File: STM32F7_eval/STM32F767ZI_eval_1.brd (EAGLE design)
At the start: 76.2 x 53.3 mm, 101 parts, among them CN3 GROVE-4P-CONN-I2C-90D, CN4 GROVE-4P-CONN-AN01-90D, CN5 ARDUINO_COMPAT_IF, CN6 STLINKV21_SWD_IF, CN7 WFT0750CZ09-SMD_, CN8 MCO_IF, CN9 UART_IF, Q1 PMF370XN_, SW1 SKRPACE010_, SW2 SKRPACE010_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

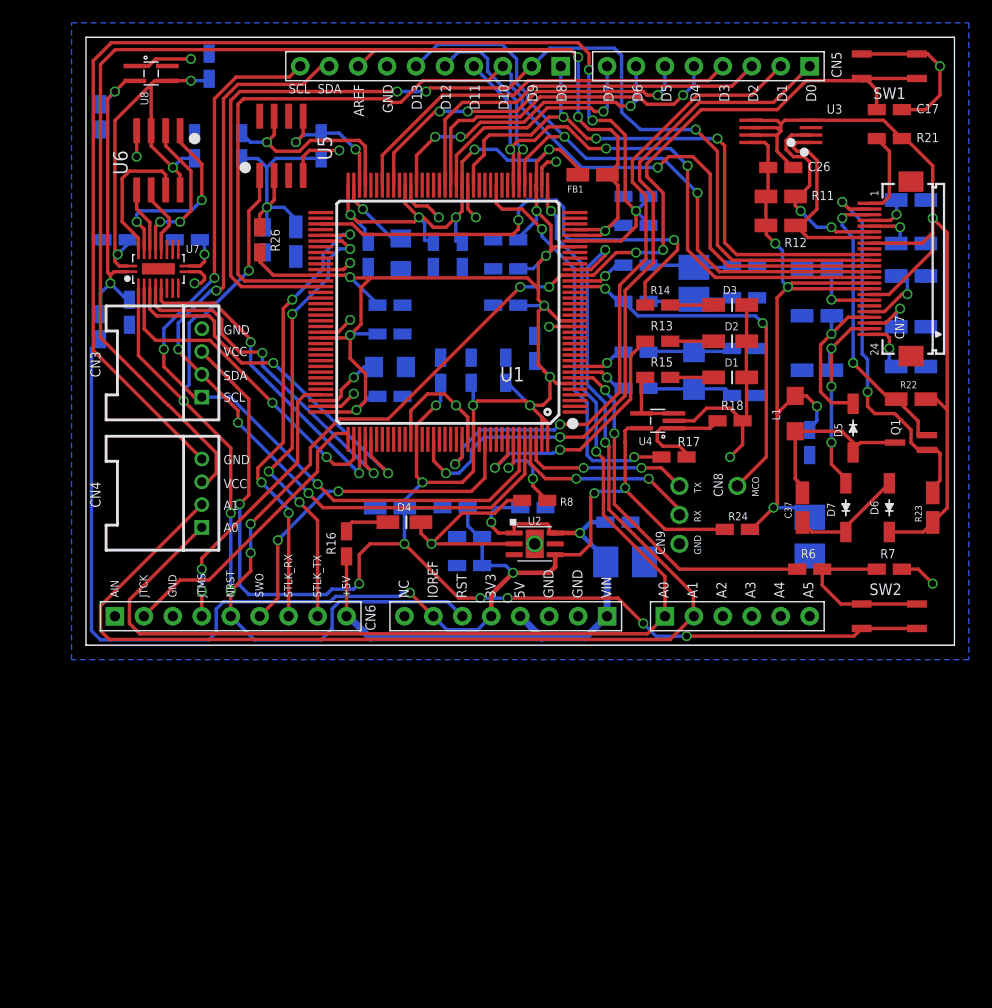
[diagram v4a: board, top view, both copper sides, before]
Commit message: 評価回路を修正
・配線を修正
・+1V8のNAMEが不正だったので修正
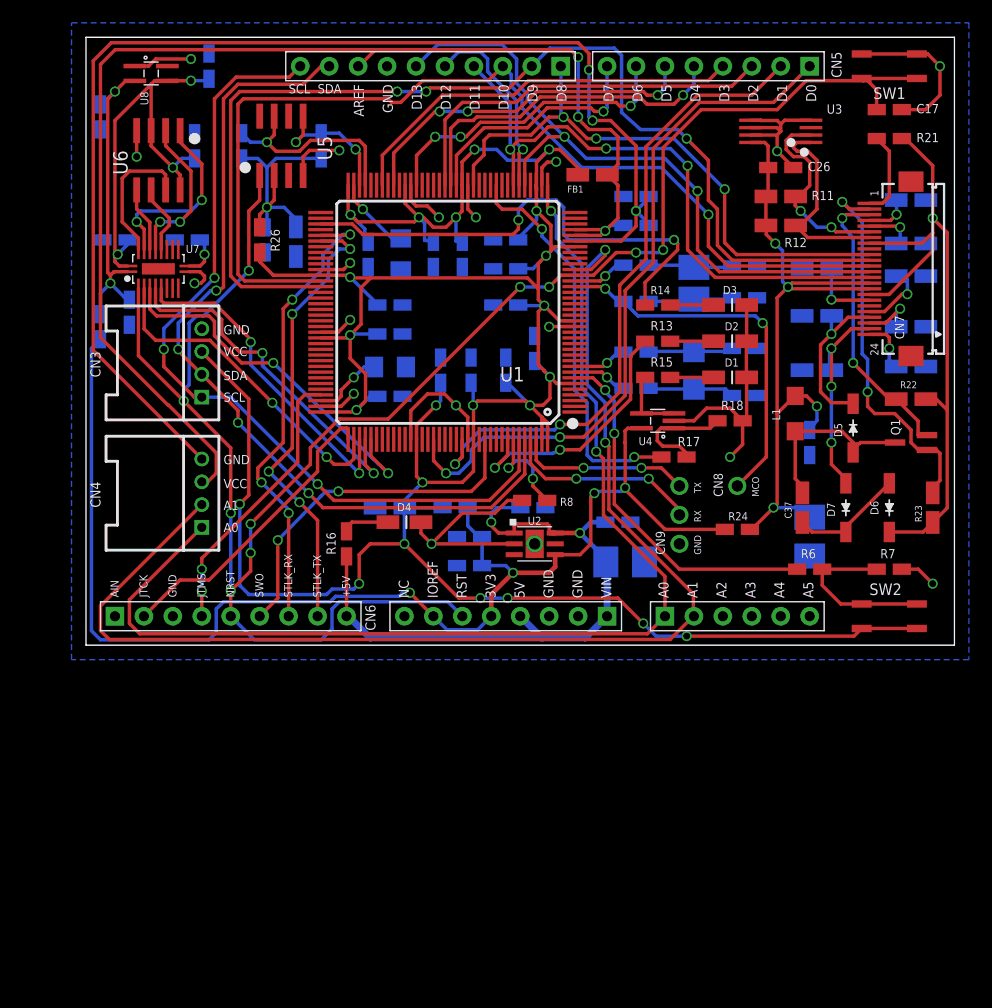
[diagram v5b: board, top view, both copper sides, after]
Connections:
- net +18V renamed +1V8
- net N$15 renamed !OE!
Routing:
- net 0V: track 189.1 -> 180.4 mm, vias 18 -> 19
- net PD14: track 92.5 -> 89.5 mm
- net PF12: track 53.5 -> 51.3 mm
- net NRST: track 171.2 -> 170.1 mm
- net PG9: track 62.9 -> 61.9 mm
- net PG14: track 58.2 -> 57.2 mm
- net PD15: track 97.1 -> 96.1 mm
- net TCK: track 26.1 -> 26.7 mm

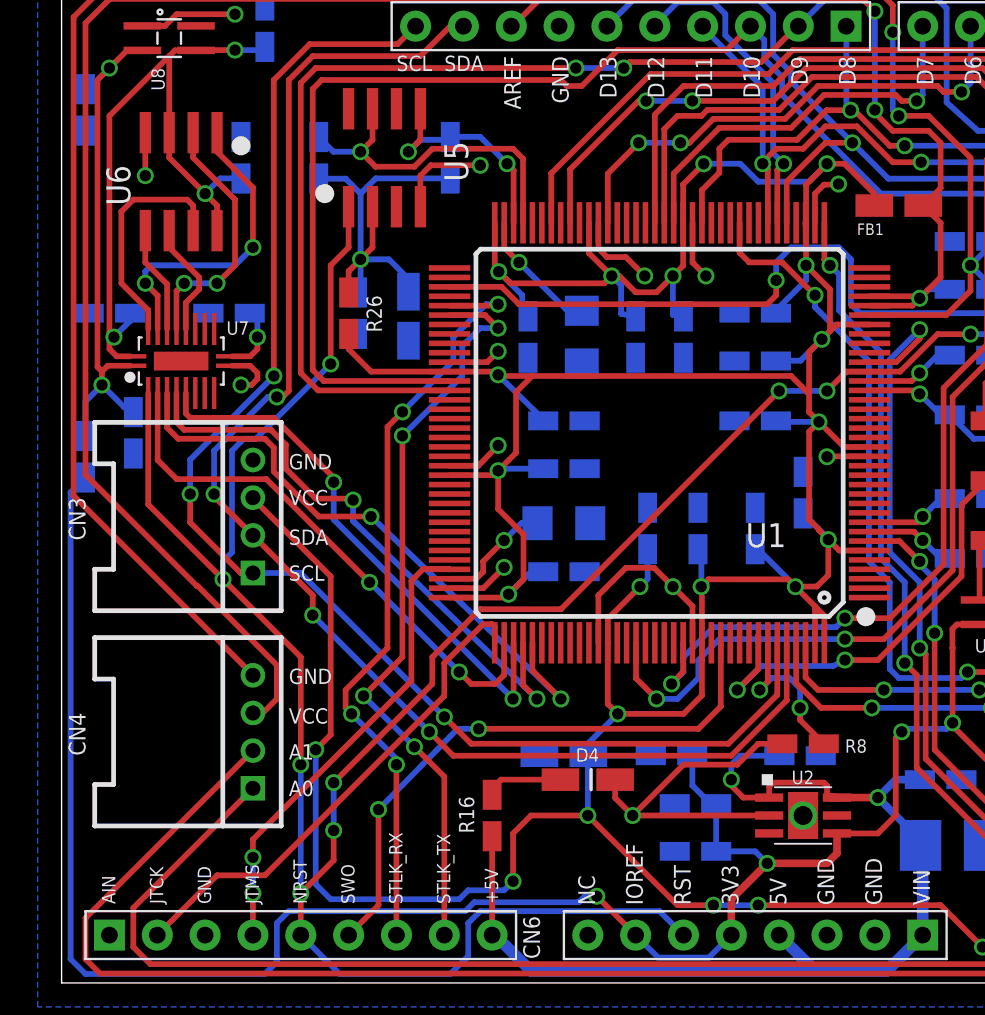
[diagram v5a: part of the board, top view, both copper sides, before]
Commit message: 評価回路を修正
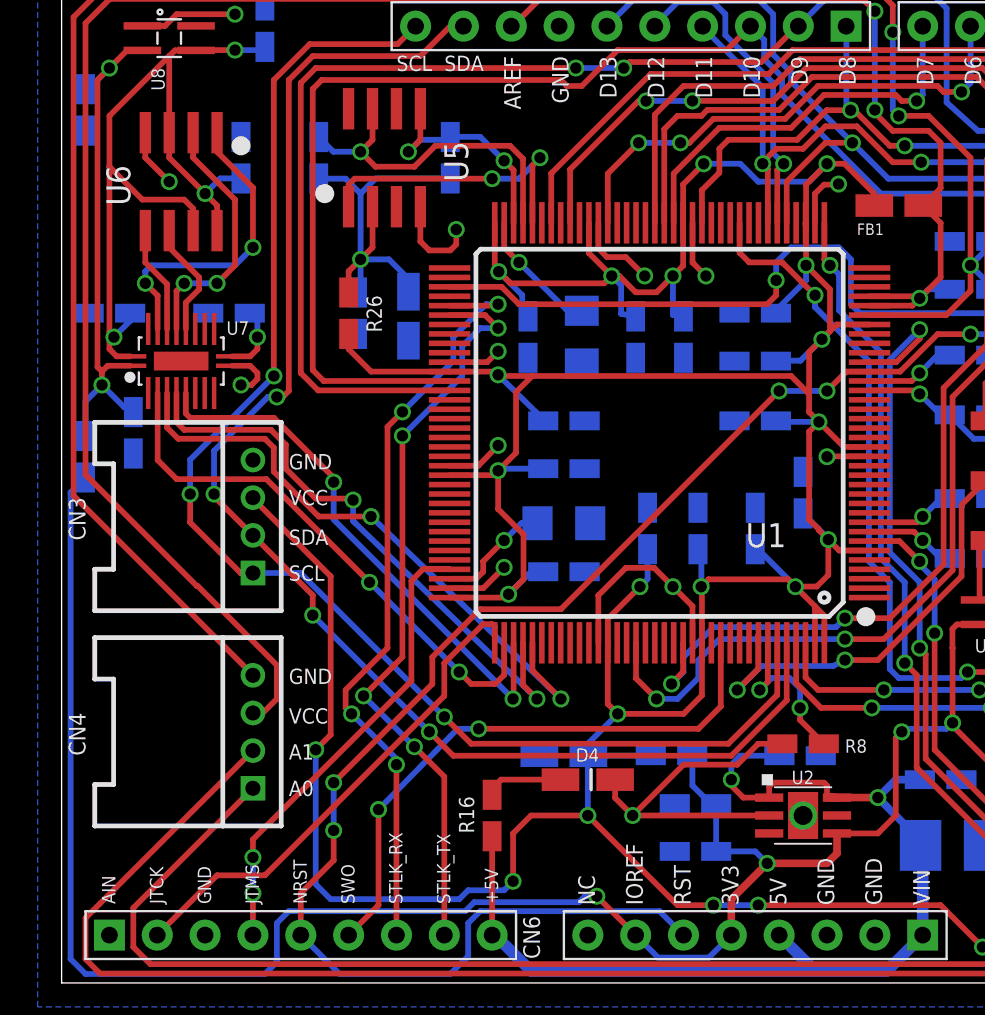
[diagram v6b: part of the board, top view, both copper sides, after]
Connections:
- removed net !RESET!: U6.7, U7.19
- new net PE15: U1.68, U5.1
- net +1V8: now also U6.7
- net NRST: no longer U5.1, U7.2
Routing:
- net NRST: track 170.1 -> 117.2 mm, vias 10 -> 6
- net PE15: track 0.00 -> 15.8 mm, vias 0 -> 2
- net !RESET!: track 12.4 -> 0.00 mm
- net +1V8: track 38.4 -> 44.9 mm
- net 0V: track 180.4 -> 181.1 mm

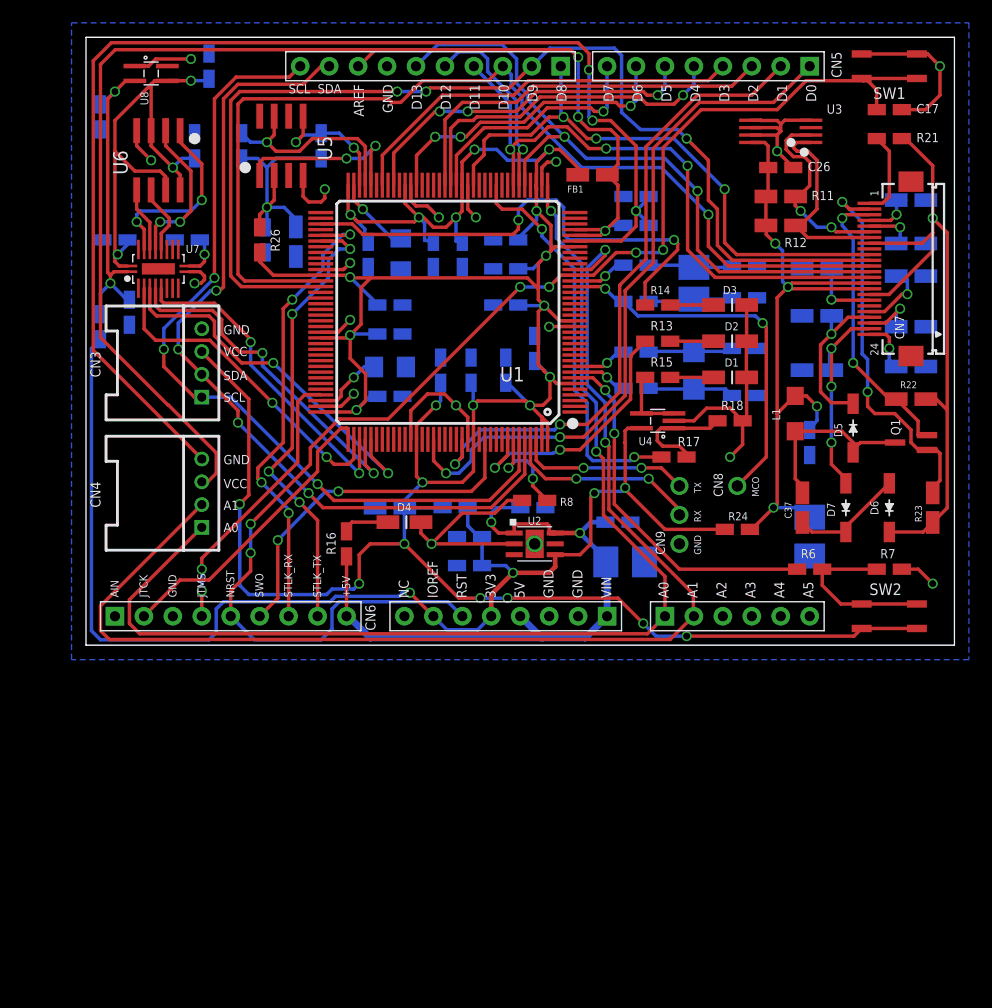
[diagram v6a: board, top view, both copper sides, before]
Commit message: 回路図を修正
・部品のパッケージを入れ替え
・セキュリティーチップ回路図のシートを移動
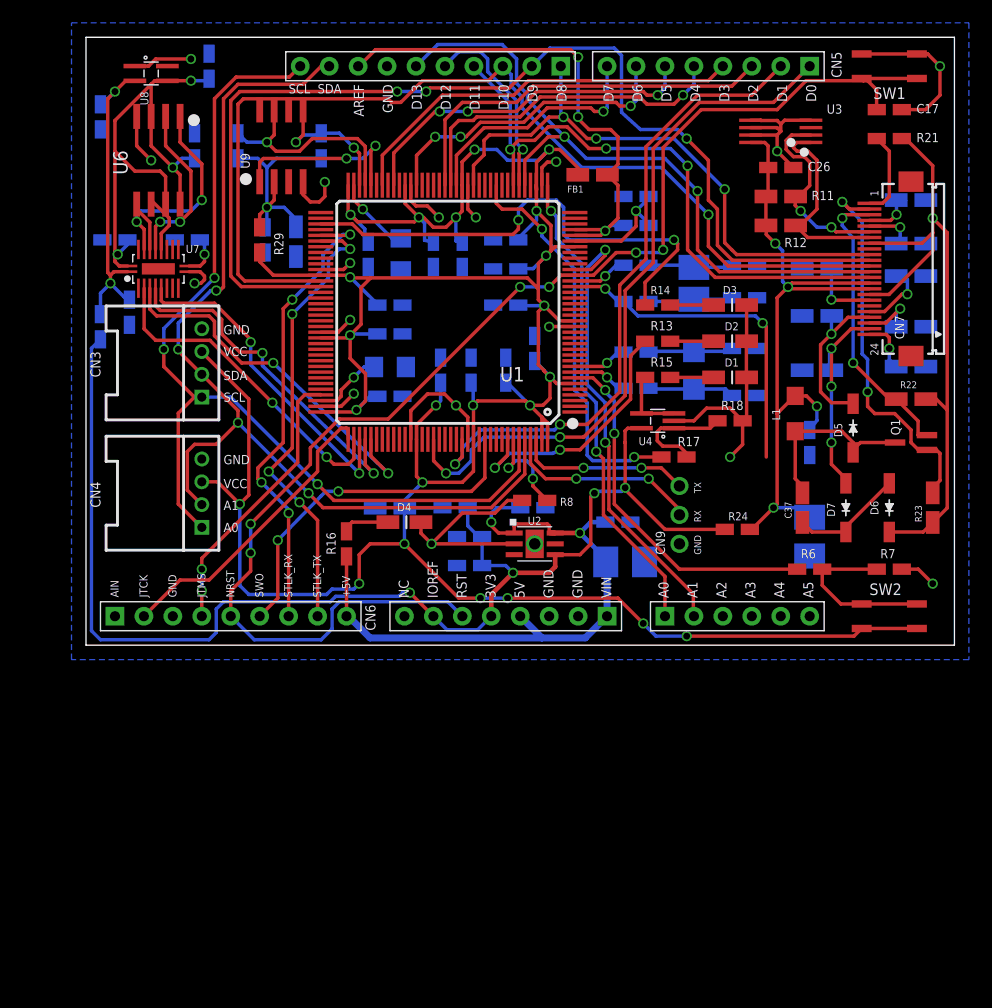
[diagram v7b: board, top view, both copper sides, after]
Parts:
- removed CN8: MCO_IF, PartsForProto:MCO_IF_1PIN
- removed R19: 3.3k, Parts:SMD_1608_DEV
- removed U5: STSAFE, Parts:SO8
- added R27: 3.3k, Parts:SMD_1608_DEV
- added U9: STSAFE, Parts:SO8N
- CN4: value GROVE-4P-CONN-AN01-90D -> GROVE-4P-CONN-I2C-90D
- U6: device Parts:SO8 -> Parts:SOP_8L
- renumbered C28 to C47, C29 to C48, R20 to R28, R26 to R29
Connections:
- net 0V: now also CN4.4, U9.4; no longer U5.4
- net AGND: no longer CN4.4
- net AVDD: no longer CN4.3
- net PA3: no longer CN4.1
- net PB10: now also R27.1, U9.7; no longer R19.1, U5.7
- net PB11: now also U9.5; no longer U5.5
- net PB8: now also CN4.1
- net PB9: now also CN4.2
- net PC0: no longer CN4.2
- net PE15: now also U9.1; no longer U5.1
- net PH0: no longer CN8.1
- net VCC_STSAFE: now also R27.2, U9.2; no longer R19.2, U5.2
- net VDD: now also CN4.3
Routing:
- net AGND: track 110.6 -> 10.7 mm, vias 3 -> 1
- net PC0: track 108.3 -> 40.4 mm
- net AVDD: track 112.9 -> 46.5 mm
- net PA3: track 101.1 -> 42.1 mm
- net PB8: track 73.9 -> 86.8 mm
- net PB9: track 75.7 -> 86.4 mm
- net VDD: track 277.9 -> 282.0 mm
- net PH0: track 33.3 -> 29.7 mm
- net +1V8: track 44.9 -> 47.4 mm
- net SO: track 13.7 -> 14.9 mm
- net SI: track 5.70 -> 4.45 mm
- net !CS!: track 16.5 -> 17.7 mm
- net 0V: track 181.1 -> 182.2 mm
- net PB10: track 18.2 -> 19.1 mm
- net PE15: track 15.8 -> 16.3 mm
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
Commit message: 回路図を修正
・構成部品を入替え
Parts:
- removed C43: 1uF, Parts:SMD_1608_DEV
- removed C44: 0.1uF, Parts:SMD_1608_DEV
- removed U8: NCP563, Parts:SC-70-4_DEV
- added C28, C49: 1uF X5R, Parts:SMD_1608_DEV
- added C29: 10uF, Parts:C1210_TPST_DEV
- added U5: MIC5366-1.8YC5_, Parts:SC-70-5_DEV
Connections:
- net !CS!: now also U7.3; no longer U7.18
- net +1V8: now also C28.1, C29.1, C45.1, U5.5, U7.1; no longer C44.1, C46.1, U7.20, U8.3
- net 0V: now also C28.2, C29.2, C49.2, U5.2; no longer C43.2, C44.2, U8.1
- net PA15: now also U7.18; no longer U7.3
- net PC10: now also U7.16; no longer U7.6
- net PC11: now also U7.14; no longer U7.5
- net PC12: now also U7.12; no longer U7.4
- net SCLK: now also U7.5; no longer U7.15
- net SI: now also U7.9; no longer U7.17
- net SO: now also U7.7; no longer U7.16
- net VCC_MEM: now also C46.1, C49.1, U5.1, U5.3, U7.20; no longer C43.1, C45.1, U7.1, U8.2
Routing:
- net VCC_MEM: track 28.2 -> 0.00 mm, vias 2 -> 0
- net +1V8: track 47.4 -> 40.9 mm, vias 3 -> 2
- net 0V: track 182.2 -> 176.6 mm, vias 19 -> 18
- net PA15: track 28.8 -> 25.2 mm
- net SI: track 4.45 -> 2.07 mm
- net SO: track 14.9 -> 12.9 mm
- net PC12: track 32.9 -> 31.1 mm
- net !CS!: track 17.7 -> 15.9 mm
- net PC11: track 31.4 -> 29.8 mm
- net SCLK: track 5.64 -> 4.23 mm
- net PC10: track 29.0 -> 27.9 mm
